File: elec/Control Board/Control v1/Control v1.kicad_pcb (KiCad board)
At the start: 2 copper layers, 126.3 x 160 mm, 178 parts, among them J1 DB9_Female_MountingHoles, J10 Conn_02x12_Odd_Even, J11 Screw_Terminal_01x02, J12 Screw_Terminal_01x02, J13 Screw_Terminal_01x02, J14 Conn_01x08, J15 DB25_Female_MountingHoles, J16 Conn_01x04, J17 Conn_01x05, J18 Conn_01x04, J19 Conn_01x07, J2 Conn_01x08, J20 Conn_01x04_Pin, J21 RJ12_6P6C_HORZ, J22 0.100_2Pin, J23 0.100_2Pin, J24 Conn_01x04, J3 Conn_01x08, J4 Conn_01x08, J5 Conn_01x08, J6 Conn_01x08, J7 Conn_02x18_Odd_Even, J8 Conn_01x10, J9 Conn_01x10, Q1 BSS138, Q10 BSS138, Q2 NCE01P30K, Q3 BSS138, Q4 BSS138, Q5 BSS138, Q6 BSS138, Q7 BSS138, Q8 BSS138, Q9 BSS138

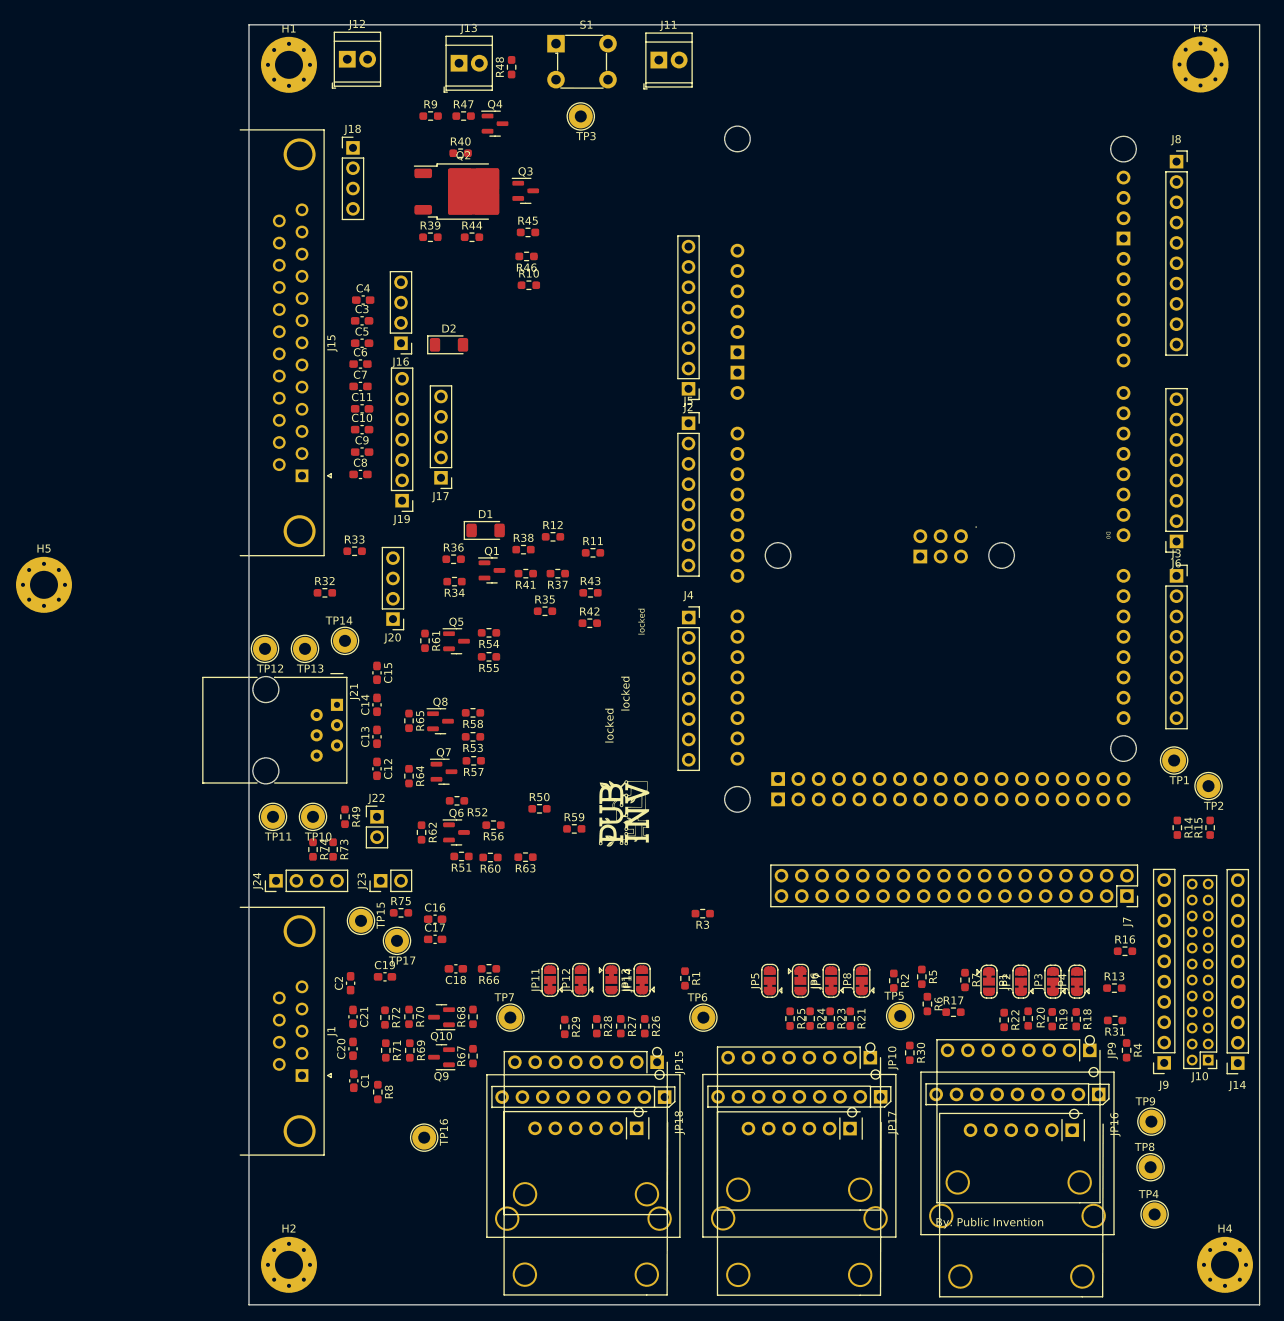
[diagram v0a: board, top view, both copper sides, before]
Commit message: Add header sockets. Refine PCB placement, temprature sensors.
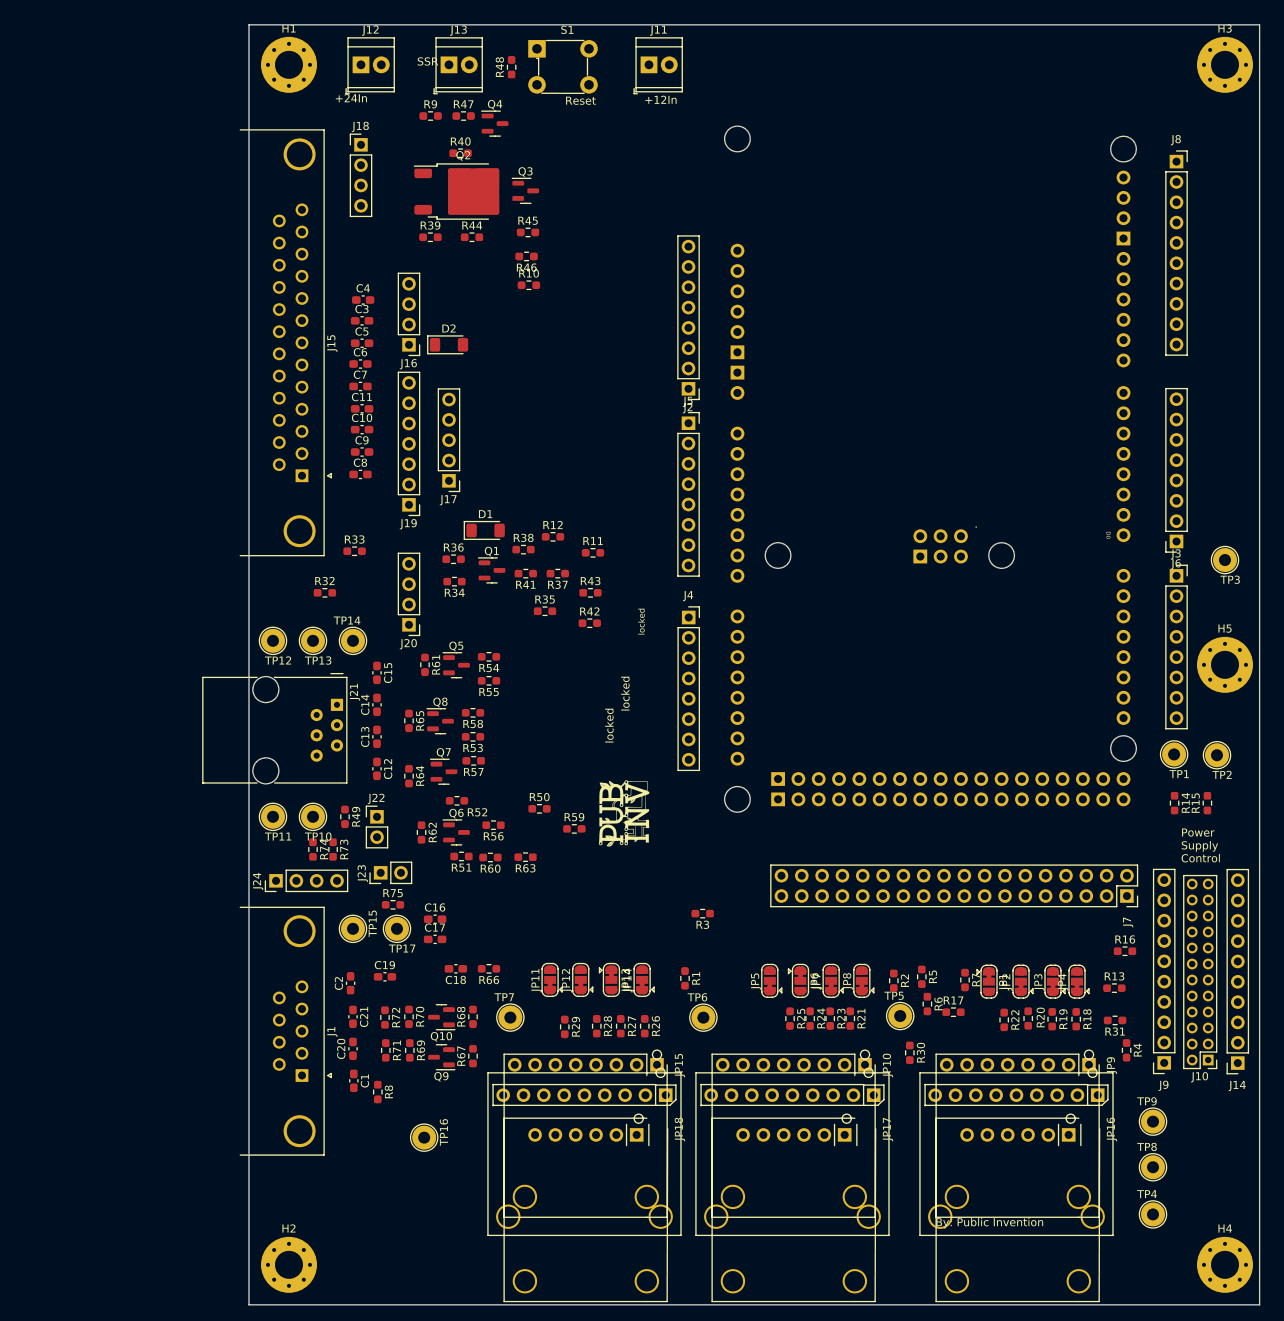
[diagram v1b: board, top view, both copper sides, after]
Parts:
- moved H5 148.0 mm to (172.0, 130.0)
- moved TP3 97.8 mm to (172.0, 116.9)
- moved TP2 4.00 mm to (171.0, 141.3)
- moved R14 3.09 mm to (165.7, 147.3)
- moved R15 3.09 mm to (169.8, 147.3)
- moved H3 3.06 mm to (172.0, 55.0)
- moved Q5 3.00 mm to (75.9, 130.1)
- moved R54 3.00 mm to (80.0, 129.0)
- moved R55 3.00 mm to (80.0, 132.0)
- moved R61 3.00 mm to (72.0, 130.0)
- moved S1 2.46 mm to (86.0, 53.0)
- moved J20 2.13 mm to (70.0, 125.0)
- moved J12 1.85 mm to (64.0, 55.0)
- moved JP9 1.81 mm to (155.0, 180.0)
- moved TP17 1.50 mm to (68.5, 163.0)
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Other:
- board text added: "+12In"
- board text added: "+24In"
- board text added: "Power Supply Control"
- board text added: "Reset"
- board text added: "SSR"

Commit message: Refine PCB placement, passives.
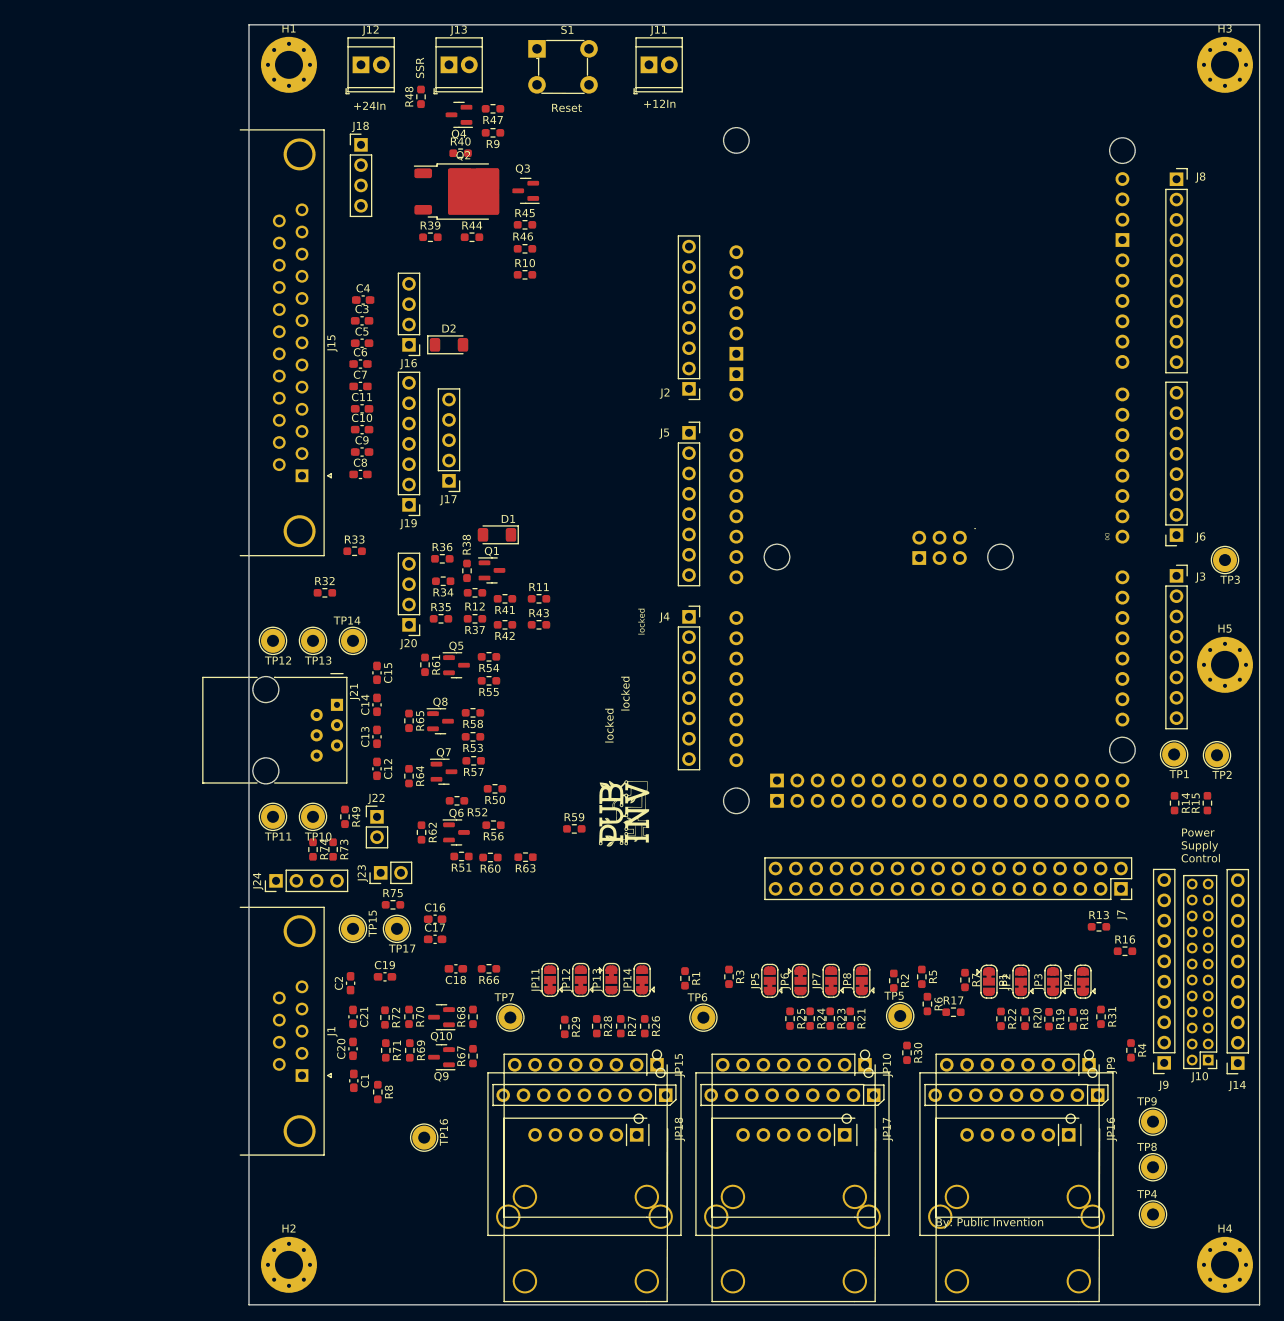
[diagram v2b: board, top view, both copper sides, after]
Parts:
- moved R35 13.0 mm to (74.0, 124.2)
- moved R12 12.0 mm to (78.2, 121.0)
- moved R48 11.9 mm to (71.5, 59.0)
- moved R37 11.8 mm to (78.2, 124.2)
- moved R42 10.6 mm to (82.0, 125.0), turned to 180 degrees
- moved R11 8.87 mm to (86.2, 121.8)
- moved R3 8.56 mm to (110.0, 169.0), turned to -90 degrees
- moved R9 8.08 mm to (80.5, 63.5), turned to 180 degrees
- moved R13 7.90 mm to (156.2, 162.8)
- moved R43 7.58 mm to (86.2, 125.0)
- moved R38 7.54 mm to (77.2, 118.2), turned to -90 degrees
- moved R50 6.10 mm to (80.8, 145.5), turned to 180 degrees
- moved Q4 4.64 mm to (76.2, 61.2), turned to 180 degrees
- moved R41 4.08 mm to (82.0, 121.8)
- moved R47 3.78 mm to (80.5, 60.5), turned to 180 degrees
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
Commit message: Net name congruancy.
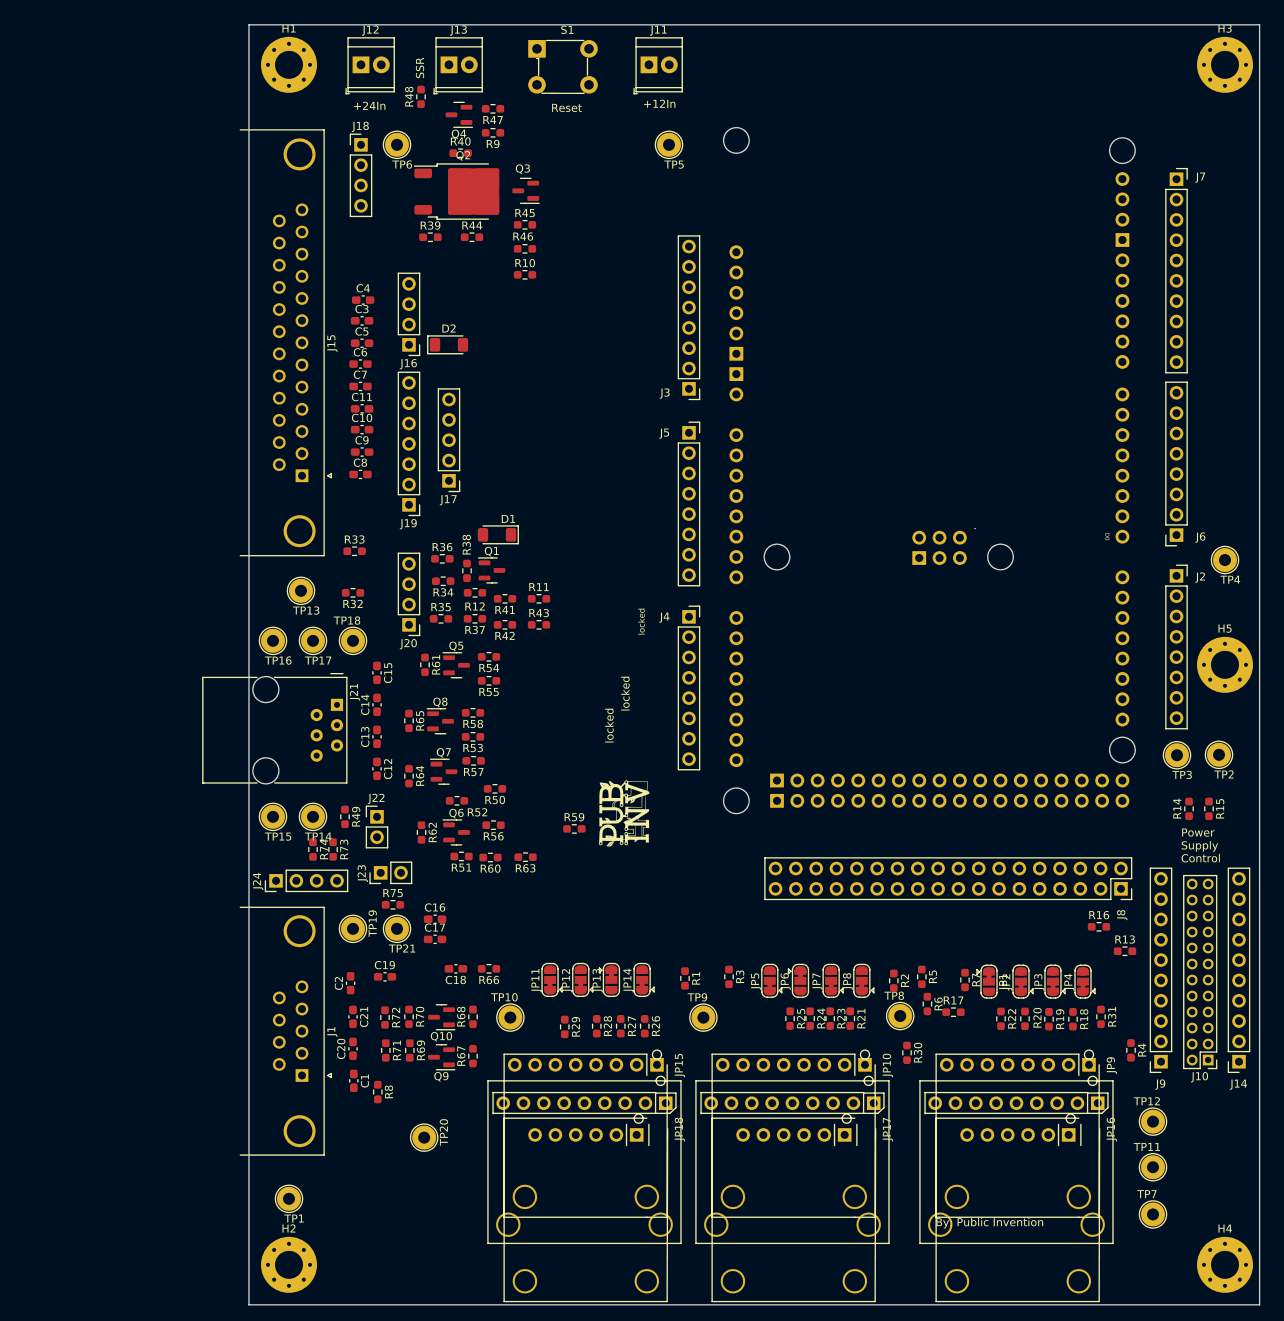
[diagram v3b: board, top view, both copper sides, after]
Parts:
- removed the J14 at (173.6, 179.8)
- added J9: Conn_01x10, Connector_PinSocket_2.54mm:PinSocket_1x10_P2.54mm_Vertical, F.Cu at (164.0, 179.6)
- added TP1: GND, TestPoint:TestPoint_Loop_D2.54mm_Drill1.5mm_Beaded, F.Cu at (55.0, 196.8)
- added TP13: GND, TestPoint:TestPoint_Loop_D2.54mm_Drill1.5mm_Beaded, F.Cu at (56.5, 120.8)
- added TP5: GND, TestPoint:TestPoint_Loop_D2.54mm_Drill1.5mm_Beaded, F.Cu at (102.5, 65.0)
- added TP6: GND, TestPoint:TestPoint_Loop_D2.54mm_Drill1.5mm_Beaded, F.Cu at (68.5, 65.0)
- A1: footprint PubInv_PCB:Arduino_Due_Shield -> Arduino:Arduino_Due_Shield
- J20: value Conn_01x04_Pin -> Conn_01x04
- R39, R40: value 10k -> 10K
- moved J14 9.35 mm to (173.8, 179.6)
- moved TP2 5.61 mm to (171.2, 141.2)
- moved TP3 5.00 mm to (166.0, 141.3)
- moved R15 4.36 mm to (170.0, 148.0)
- moved R32 3.51 mm to (63.0, 121.0), turned to 180 degrees
- moved R14 2.41 mm to (167.5, 148.0)
- moved JP19 1.00 mm to (158.0, 182.0)
- moved JP20 1.00 mm to (130.0, 182.0)
- moved JP21 1.00 mm to (104.0, 182.0)
- renumbered J9 to J14, J3 to J2, J2 to J3, J8 to J7, J7 to J8, R16 to R13, R15 to R14, R14 to R15, R13 to R16, TP7 to TP10, TP8 to TP11, TP9 to TP12, TP10 to TP14, TP11 to TP15, TP12 to TP16, TP13 to TP17, TP14 to TP18, TP15 to TP19, TP1 to TP2, TP16 to TP20, TP17 to TP21, TP2 to TP3, TP3 to TP4, TP4 to TP7, TP5 to TP8, TP6 to TP9
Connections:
- J10 pad 1: /VO+ -> /VS+
- J10 pad 10: /EN- -> GND
- J10 pad 11: /AUX -> /EN+
- J10 pad 12: /EN+ -> /AUX
- J10 pad 13: GND -> /ACI
- J10 pad 14: /ACI -> GND
- J10 pad 15: GND -> /VCI
- J10 pad 16: /VCI -> GND
- J10 pad 17: GND -> /AUX
- J10 pad 18: /AUX -> GND
- J10 pad 2: /VS+ -> /VO+
- J10 pad 21: GND -> /AUX
- J10 pad 22: /AUX -> GND
- J10 pad 23: /TX -> /RX
- J10 pad 24: /RX -> /TX
- J10 pad 3: /VO- -> /VS-
- J10 pad 4: /VS- -> /VO-
- J10 pad 5: GND -> /POK
- J10 pad 6: /POK -> GND
- J10 pad 7: /VSET -> /PAR
- J10 pad 8: /PAR -> /VSET
- J10 pad 9: GND -> /EN-
- J2 pad 7: D23 -> SDA
- J2 pad 8: D22 -> SCL
- R13 pad 1: Net-(J10-Pin_19) -> Net-(J10-Pin_20)
- R16 pad 2: Net-(J10-Pin_20) -> Net-(J10-Pin_19)

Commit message: Net name congruancy to D35. Add named test points.
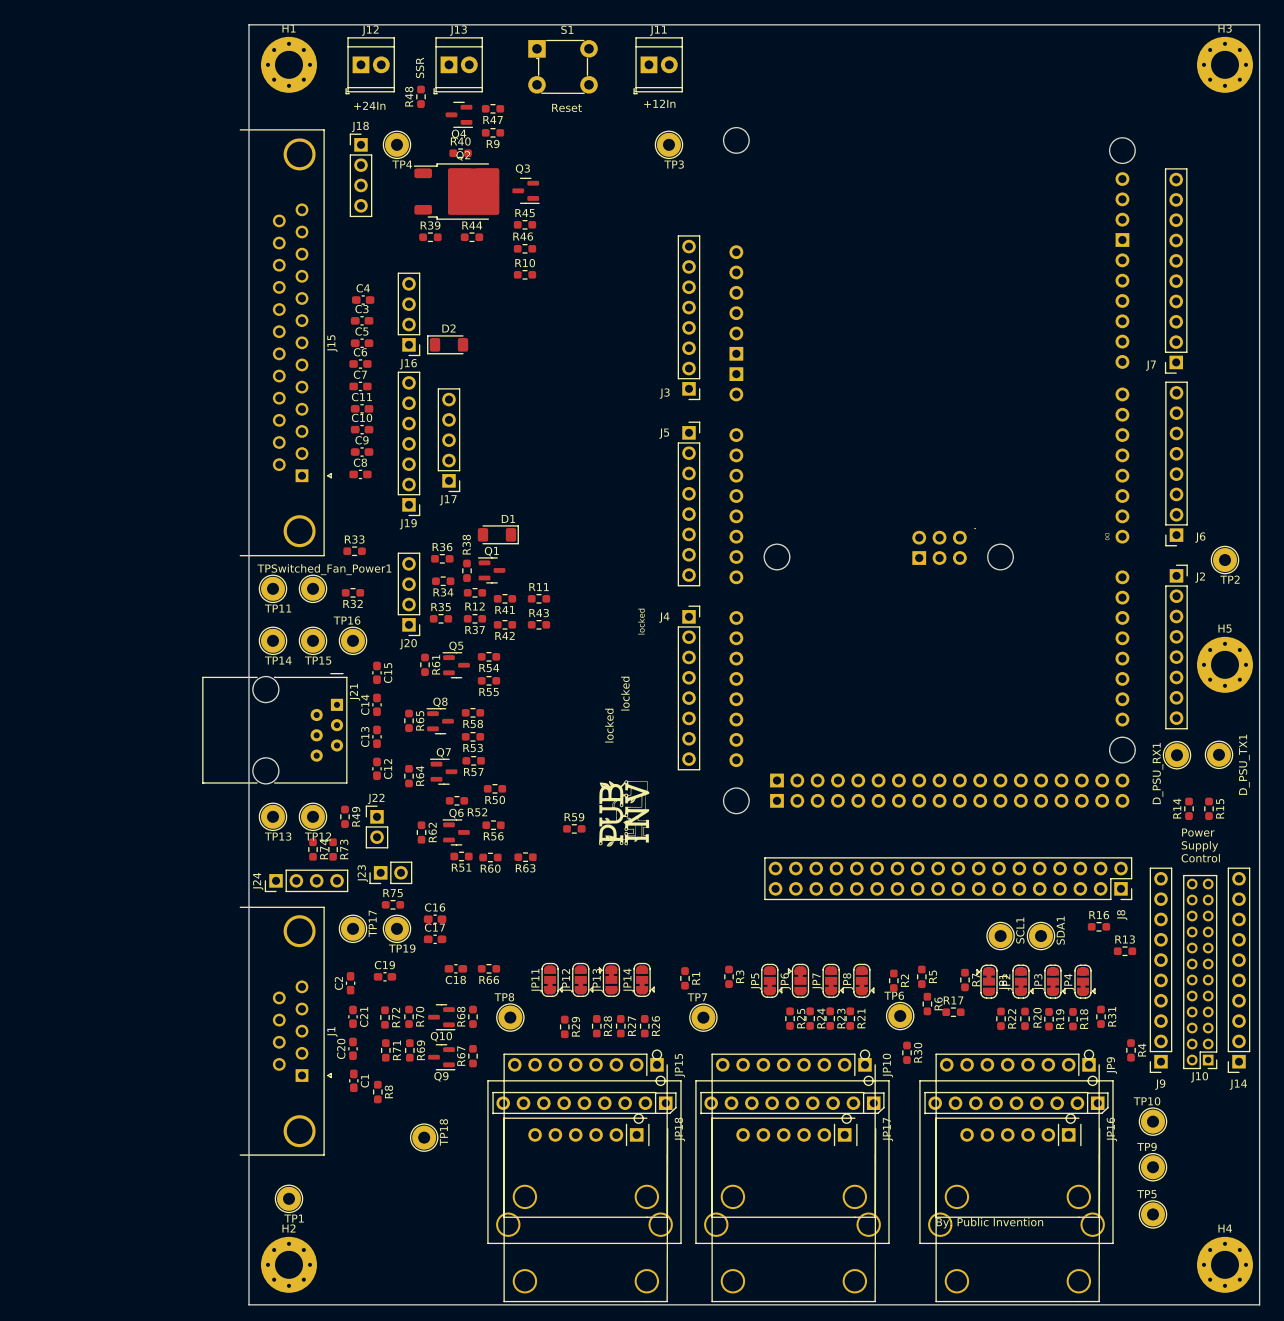
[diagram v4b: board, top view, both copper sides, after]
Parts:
- added SCL1: SCL, TestPoint:TestPoint_Loop_D2.54mm_Drill1.5mm_Beaded, F.Cu at (143.9, 163.9)
- added SDA1: SDA, TestPoint:TestPoint_Loop_D2.54mm_Drill1.5mm_Beaded, F.Cu at (149.0, 163.9)
- added TPSwitched_Fan_Power1: Switched_Fan_Power, TestPoint:TestPoint_Loop_D2.54mm_Drill1.5mm_Beaded, F.Cu at (58.0, 120.5)
- D_PSU_RX1: renamed from TP3; value RX -> D_PSU_RX
- D_PSU_TX1: renamed from TP2; value TX -> D_PSU_TX
- moved J7 22.9 mm to (165.9, 92.2), turned to 180 degrees
- moved TP11 3.51 mm to (53.0, 120.5)
- renumbered TP12 to TP10, TP13 to TP11, TP14 to TP12, TP15 to TP13, TP16 to TP14, TP17 to TP15, TP18 to TP16, TP19 to TP17, TP20 to TP18, TP21 to TP19, TP4 to TP2, TP5 to TP3, TP6 to TP4, TP7 to TP5, TP8 to TP6, TP9 to TP7, TP10 to TP8, TP11 to TP9
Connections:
- A1 pad D11: Net-(J7-Pin_7) -> Net-(J7-Pin_4)
- A1 pad D12: Net-(J7-Pin_6) -> Net-(J7-Pin_5)
- A1 pad D13: Net-(J7-Pin_5) -> Net-(J7-Pin_6)
- A1 pad D8: Net-(J7-Pin_10) -> Net-(J7-Pin_1)
- A1 pad D9: BLOWER_PWM -> nFAN1_PWM
- J7 pad 1: SCL1 -> Net-(J7-Pin_1)
- J7 pad 10: Net-(J7-Pin_10) -> SCL1
- J7 pad 2: SDA1 -> nFAN1_PWM
- J7 pad 3: AREF -> Net-(A1-D10_CS0)
- J7 pad 4: GND -> Net-(J7-Pin_4)
- J7 pad 7: Net-(J7-Pin_7) -> GND
- J7 pad 8: Net-(A1-D10_CS0) -> AREF
- J7 pad 9: BLOWER_PWM -> SDA1
- R12 pad 2: BLOWER_PWM -> nFAN1_PWM
